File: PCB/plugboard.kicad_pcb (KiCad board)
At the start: 2 copper layers, 100 x 100 mm, 96 parts, among them J1 1/4" Jack, J10 1/4" Jack, J11 Conn_01x19_Male_0, J2 1/4" Jack, J3 1/4" Jack, J4 1/4" Jack, J5 1/4" Jack, J6 1/4" Jack, J7 Conn_01x19_Male_0, J8 1/4" Jack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

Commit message: Final rev
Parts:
- added G***: LOGO, enigmaprints:damn4, B.Cu at (140.1, 90.6)
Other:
- board text added: "1 2 2 1 2 1 2 1 2 1 2 1 2 1 2 1 2 VCC GND"
- board text added: "2 3"
- board text added: "A2 A1 A0"
- board text added: "Alphabet Resistor Line (1K Ohm)"
- board text added: "CS EN VCC"
- board text added: "Corey Cochran-Lepiz Bryce Mann"
- board text added: "Enigma Plugboard"
- board text added: "GND GND GND"
- board text added: "Sig A4 A3"
- board text added: "Team Enigma Principles of Engineering Fall 2018"

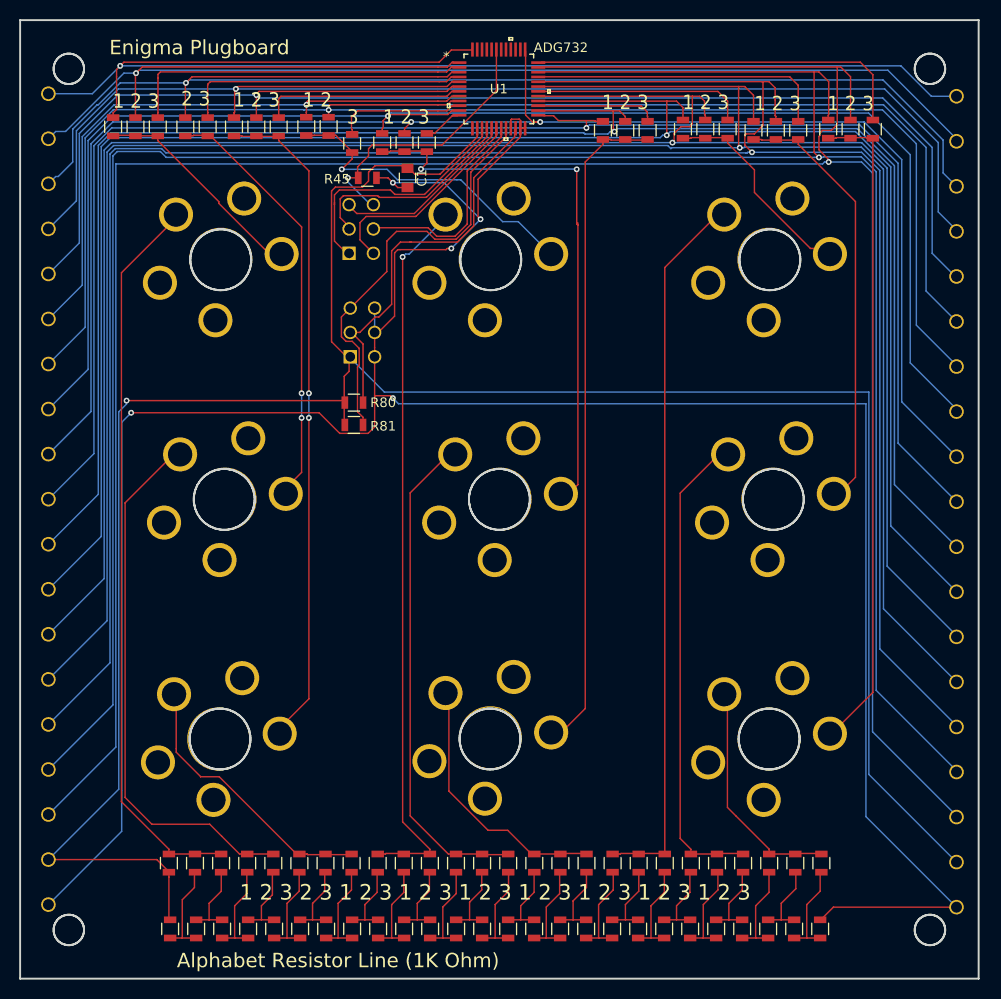
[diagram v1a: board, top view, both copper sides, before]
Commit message: Final plugboard
Added a bit more tolerance on the jack_hole footprint
Fix layout to accomodate for tip ring usage
Made silkscreen a bit more clear
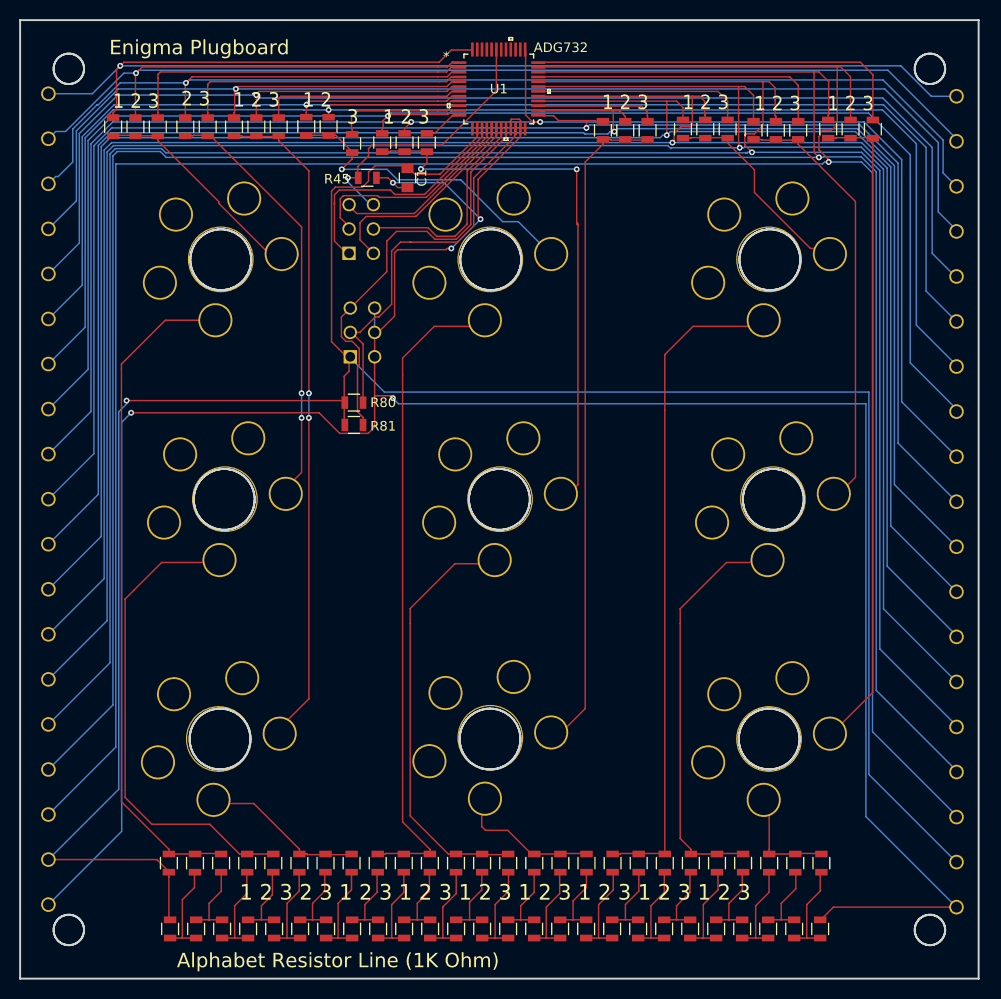
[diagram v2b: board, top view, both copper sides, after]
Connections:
- R27 pad 1: Net-(J1-Pad1) -> Net-(J1-Pad2)
- R28 pad 1: Net-(J1-Pad1) -> Net-(J1-Pad2)
- R29 pad 1: Net-(J1-Pad1) -> Net-(J1-Pad2)
- R30 pad 1: Net-(J2-Pad1) -> Net-(J2-Pad2)
- R31 pad 1: Net-(J2-Pad1) -> Net-(J2-Pad2)
- R32 pad 1: Net-(J2-Pad1) -> Net-(J2-Pad2)
- R33 pad 1: Net-(J3-Pad1) -> Net-(J3-Pad2)
- R34 pad 1: Net-(J3-Pad1) -> Net-(J3-Pad2)
- R35 pad 1: Net-(J3-Pad1) -> Net-(J3-Pad2)
- R46 pad 2: Net-(J4-Pad1) -> Net-(J4-Pad2)
- R47 pad 2: Net-(J4-Pad1) -> Net-(J4-Pad2)
- R48 pad 2: Net-(J5-Pad1) -> Net-(J5-Pad2)
- R49 pad 2: Net-(J5-Pad1) -> Net-(J5-Pad2)
- R50 pad 2: Net-(J5-Pad1) -> Net-(J5-Pad2)
- R51 pad 2: Net-(J6-Pad1) -> Net-(J6-Pad2)
- R52 pad 2: Net-(J6-Pad1) -> Net-(J6-Pad2)
- R53 pad 2: Net-(J6-Pad1) -> Net-(J6-Pad2)
- R62 pad 2: Net-(J8-Pad1) -> Net-(J8-Pad2)
- R63 pad 2: Net-(J8-Pad1) -> Net-(J8-Pad2)
- R64 pad 2: Net-(J8-Pad1) -> Net-(J8-Pad2)
- R65 pad 2: Net-(J9-Pad1) -> Net-(J9-Pad2)
- R66 pad 2: Net-(J9-Pad1) -> Net-(J9-Pad2)
- R67 pad 2: Net-(J9-Pad1) -> Net-(J9-Pad2)
- R68 pad 2: Net-(J10-Pad1) -> Net-(J10-Pad2)
- R69 pad 2: Net-(J10-Pad1) -> Net-(J10-Pad2)
- R70 pad 2: Net-(J10-Pad1) -> Net-(J10-Pad2)
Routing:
- net Net-(J1-Pad1): track 75.6 -> 0.00 mm
- net Net-(J2-Pad1): track 74.9 -> 0.00 mm, vias 1 -> 0
- net Net-(J3-Pad1): track 73.5 -> 0.00 mm
- net Net-(J1-Pad2): track 0.00 -> 68.5 mm
- net Net-(J3-Pad2): track 0.00 -> 67.5 mm
- net Net-(J2-Pad2): track 0.00 -> 66.9 mm
- net Net-(J4-Pad1): track 54.8 -> 0.00 mm
- net Net-(J5-Pad1): track 50.6 -> 0.63 mm
- net Net-(J6-Pad1): track 49.4 -> 0.00 mm
- net Net-(J4-Pad2): track 0.00 -> 48.5 mm
- net Net-(J5-Pad2): track 0.00 -> 42.7 mm
- net Net-(J6-Pad2): track 0.00 -> 41.1 mm
- net Net-(J8-Pad1): track 27.2 -> 0.00 mm
- net Net-(J9-Pad1): track 26.0 -> 0.00 mm
- net Net-(J10-Pad1): track 23.5 -> 0.50 mm
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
